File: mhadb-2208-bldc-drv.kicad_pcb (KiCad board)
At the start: 2 copper layers, 45 x 40 mm, 69 parts, among them J1 TC2030, J2 Conn_01x04, J3 Conn_01x04_Pin, M1 Motor_3_Phases, SW1 SW_Push, SW2 SW_Push, SW3 SW_Push, U1 SN65HVD230, U2 STM32F103C8Tx, U3 DRV8311H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

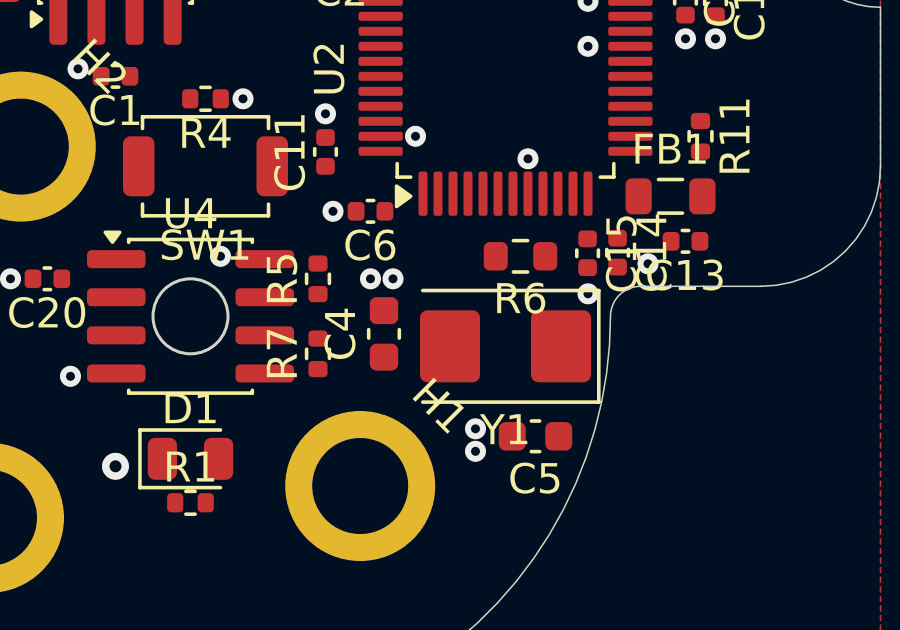
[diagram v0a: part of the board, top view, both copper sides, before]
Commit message: pcb: route crystal
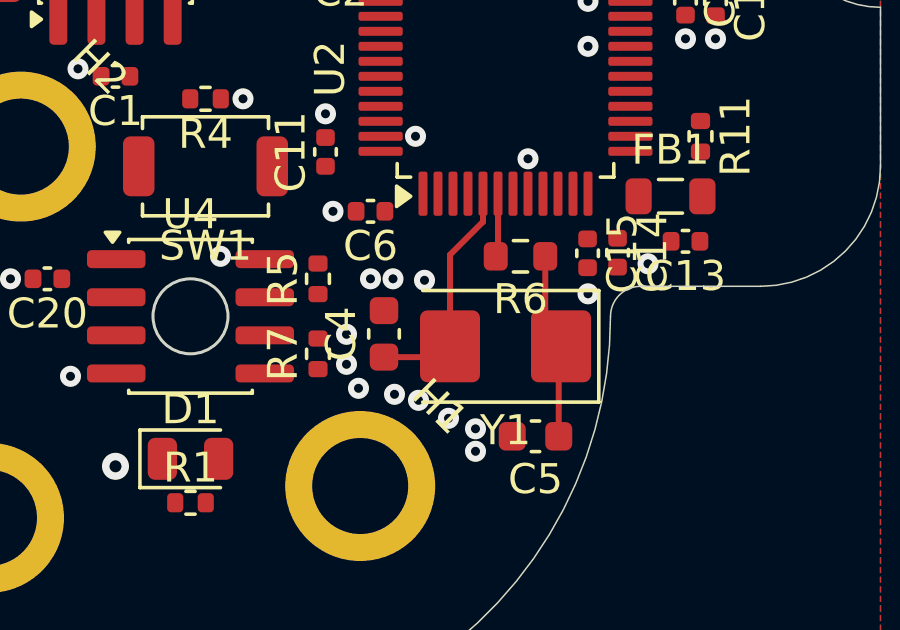
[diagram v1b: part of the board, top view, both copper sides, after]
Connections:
- U2 pad 25: /BTN1 -> unconnected-(U2-PB12-Pad25)
- U2 pad 41: unconnected-(U2-PB5-Pad41) -> /BTN1
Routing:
- net /XTAL_I: track 0.00 -> 7.89 mm
- net /XTAL_RO: track 0.00 -> 6.25 mm
- net /XTAL_O: track 0.00 -> 2.12 mm
- net GND: vias 53 -> 60
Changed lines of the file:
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@@
 	(net 41 "/SOB")
 	(net 42 "unconnected-(U1-Vref-Pad5)")
-	(net 43 "unconnected-(U2-PB5-Pad41)")
+	(net 43 "unconnected-(U2-PB12-Pad25)")
 	(net 44 "unconnected-(U2-PA7-Pad17)")
 	(net 45 "unconnected-(U2-PC13-Pad2)")
@@
 			(layers "F.Cu" "F.Mask" "F.Paste")
 			(roundrect_rratio 0.25)
-			(net 39 "/BTN1")
+			(net 43 "unconnected-(U2-PB12-Pad25)")
 			(pinfunction "PB12")
-			(pintype "bidirectional")
+			(pintype "bidirectional+no_connect")
 		)
 		(pad "26" smd roundrect
@@
 			(layers "F.Cu" "F.Mask" "F.Paste")
 			(roundrect_rratio 0.25)
-			(net 43 "unconnected-(U2-PB5-Pad41)")
+			(net 39 "/BTN1")
 			(pinfunction "PB5")
-			(pintype "bidirectional+no_connect")
+			(pintype "bidirectional")
 		)
 		(pad "42" smd roundrect
@@
 	)
 	(via
+		(at 124.6 88.4)
+		(size 0.7)
+		(drill 0.3)
+		(layers "F.Cu" "B.Cu")
+		(free yes)
+		(net 2)
+	)
+	(via
 		(at 120.75 78.75)
 		(size 0.7)
@@
 	)
 	(via
+		(at 127.6 89.4)
+		(size 0.7)
+		(drill 0.3)
+		(layers "F.Cu" "B.Cu")
+		(free yes)
+		(net 2)
+	)
+	(via
 		(at 124 70.5)
 		(size 0.9)
@@
 	)
 	(via
+		(at 124.2 86.6)
+		(size 0.7)
+		(drill 0.3)
+		(layers "F.Cu" "B.Cu")
+		(free yes)
+		(net 2)
+	)
+	(via
 		(at 134.25 65)
 		(size 0.7)
@@
 	)
 	(via
+		(at 126.8 84.8)
+		(size 0.7)
+		(drill 0.3)
+		(layers "F.Cu" "B.Cu")
+		(free yes)
+		(net 2)
+	)
+	(via
 		(at 102.25 76.25)
 		(size 0.7)
@@
 	)
 	(via
+		(at 124.2 87.6)
+		(size 0.7)
+		(drill 0.3)
+		(layers "F.Cu" "B.Cu")
+		(free yes)
+		(net 2)
+	)
+	(via
 		(at 128.5 90.5)
 		(size 0.7)
@@
 	)
 	(via
+		(at 126.6 88.8)
+		(size 0.7)
+		(drill 0.3)
+		(layers "F.Cu" "B.Cu")
+		(free yes)
+		(net 2)
+	)
+	(via
 		(at 105.25 70.5)
 		(size 0.7)
@@
 		(net 2)
 	)
+	(via
+		(at 125.8 88.6)
+		(size 0.7)
+		(drill 0.3)
+		(layers "F.Cu" "B.Cu")
+		(free yes)
+		(net 2)
+	)
+	(segment
+		(start 128.75 82.85)
+		(end 127.65 83.95)
+		(width 0.2)
+		(layer "F.Cu")
+		(net 5)
+	)
+	(segment
+		(start 127.65 83.95)
+		(end 127.65 87)
+		(width 0.2)
+		(layer "F.Cu")
+		(net 5)
+	)
+	(segment
+		(start 127.29 87.36)
+		(end 127.65 87)
+		(width 0.2)
+		(layer "F.Cu")
+		(net 5)
+	)
+	(segment
+		(start 128.75 81.9125)
+		(end 128.75 82.85)
+		(width 0.2)
+		(layer "F.Cu")
+		(net 5)
+	)
+	(segment
+		(start 125.45 87.36)
+		(end 127.29 87.36)
+		(width 0.2)
+		(layer "F.Cu")
+		(net 5)
+	)
+	(segment
+		(start 130.825 86.475)
+		(end 131.35 87)
+		(width 0.2)
+		(layer "F.Cu")
+		(net 6)
+	)
+	(segment
+		(start 131.275 87.075)
+		(end 131.35 87)
+		(width 0.2)
+		(layer "F.Cu")
+		(net 6)
+	)
+	(segment
+		(start 131.275 90)
+		(end 131.275 87.075)
+		(width 0.2)
+		(layer "F.Cu")
+		(net 6)
+	)
+	(segment
+		(start 130.825 84)
+		(end 130.825 86.475)
+		(width 0.2)
+		(layer "F.Cu")
+		(net 6)
+	)
+	(segment
+		(start 129.25 81.9125)
+		(end 129.25 83.925)
+		(width 0.2)
+		(layer "F.Cu")
+		(net 27)
+	)
+	(segment
+		(start 129.25 83.925)
+		(end 129.175 84)
+		(width 0.2)
+		(layer "F.Cu")
+		(net 27)
+	)
 	(zone

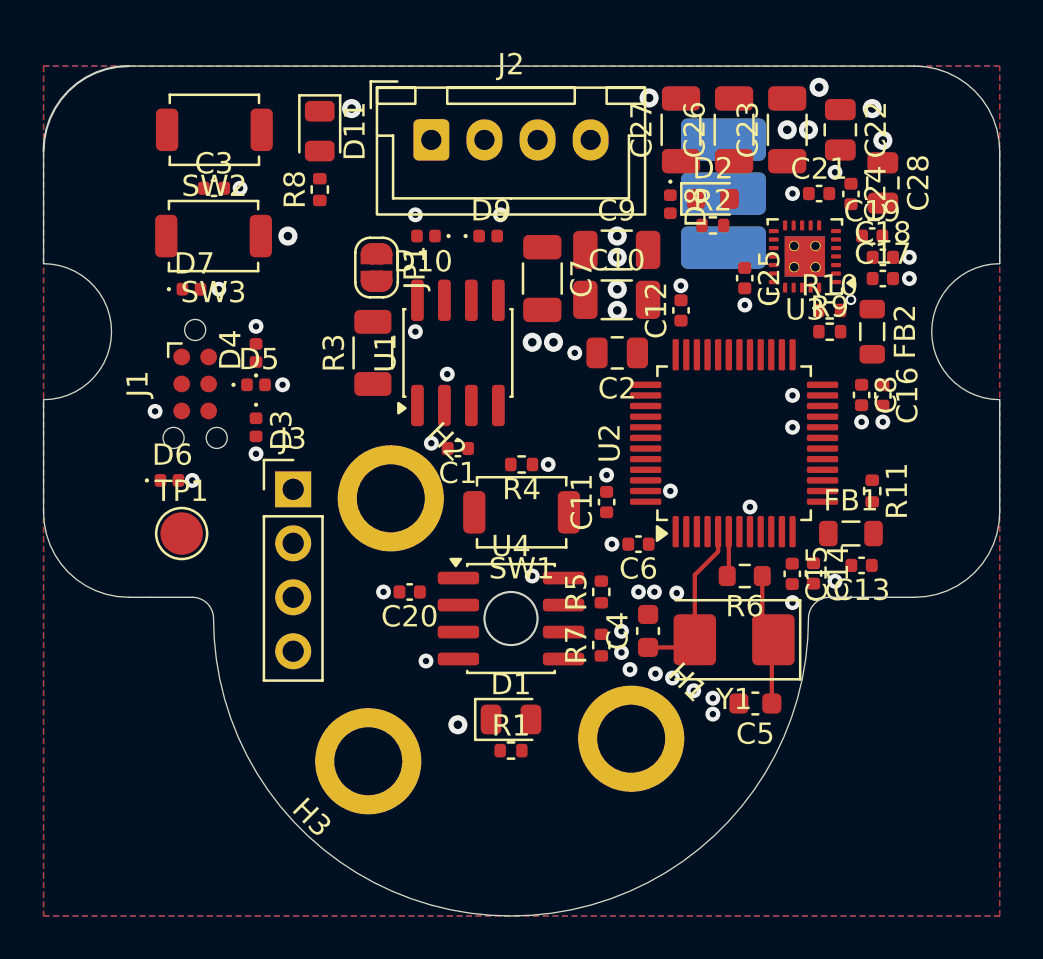
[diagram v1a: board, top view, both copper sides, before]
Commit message: pcb: route SWD
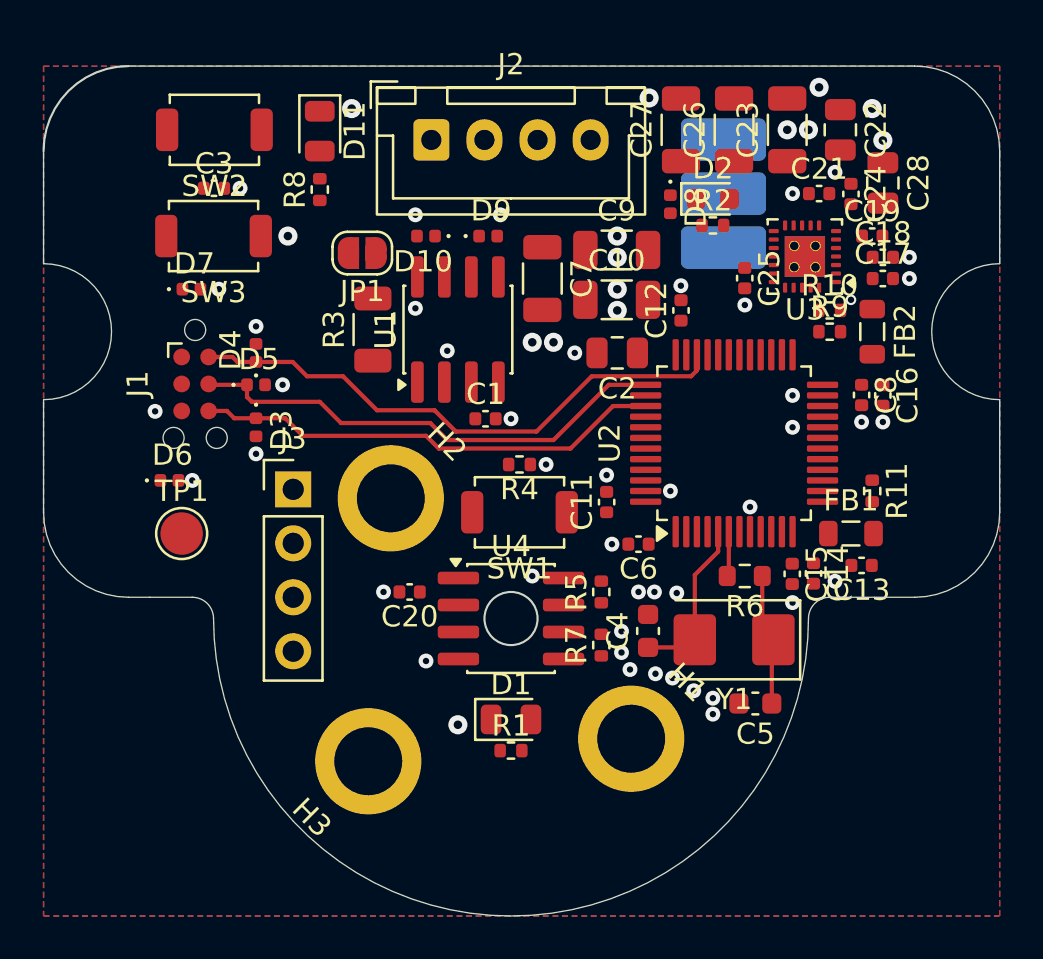
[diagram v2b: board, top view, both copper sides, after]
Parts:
- moved C1 1.91 mm to (117.8, 76.6), turned to 0 degrees
- moved R3 1.10 mm to (112.5, 72.4)
- moved U1 1.10 mm to (116.5, 72.4)
- moved JP1 0.96 mm to (112.0, 68.8), turned to 180 degrees
- moved R4 0.10 mm to (119.4, 78.8)
- moved SW1 0.10 mm to (119.4, 81.0)
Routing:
- net /SWDIO: track 0.00 -> 26.4 mm
- net /SWCLK: track 0.00 -> 23.1 mm
- net /SWO: track 0.00 -> 22.1 mm

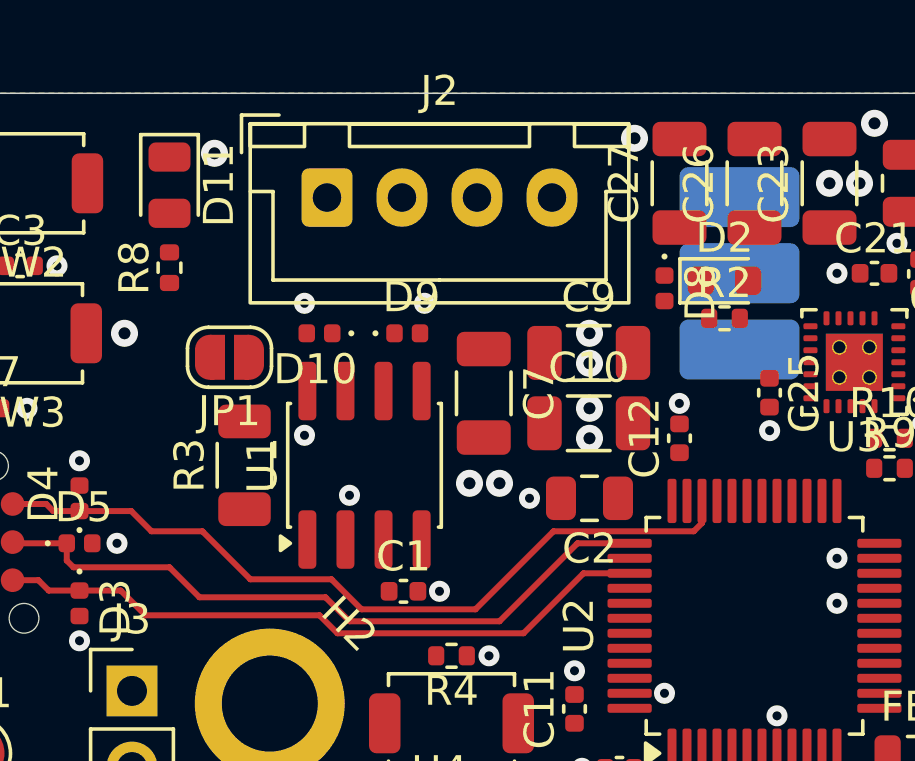
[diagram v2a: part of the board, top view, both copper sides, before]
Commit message: pcb: route CAN
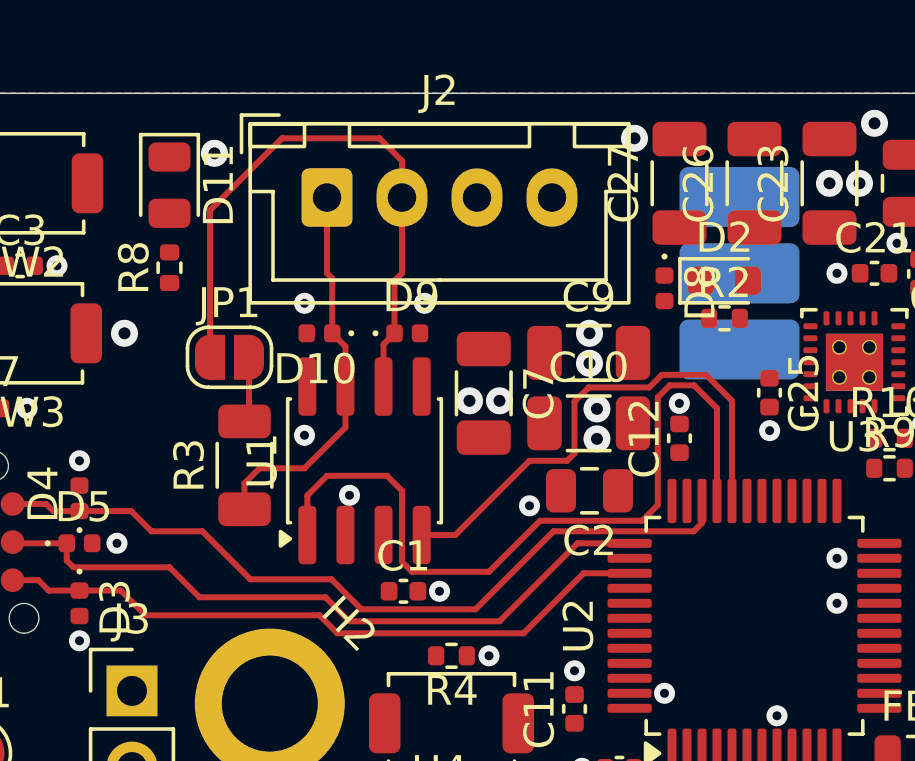
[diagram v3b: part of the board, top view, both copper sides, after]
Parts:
- moved C2 0.25 mm to (124.0, 73.2)
- moved U1 0.15 mm to (116.5, 72.2)
- turned JP1 to 0 degrees
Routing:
- net /CAN_TX: track 0.00 -> 26.0 mm
- net /CANL: track 0.00 -> 20.5 mm
- net /CAN_RX: track 0.00 -> 17.3 mm
- net /CANH: track 0.00 -> 13.1 mm
- net Net-(JP1-B): track 0.00 -> 2.41 mm

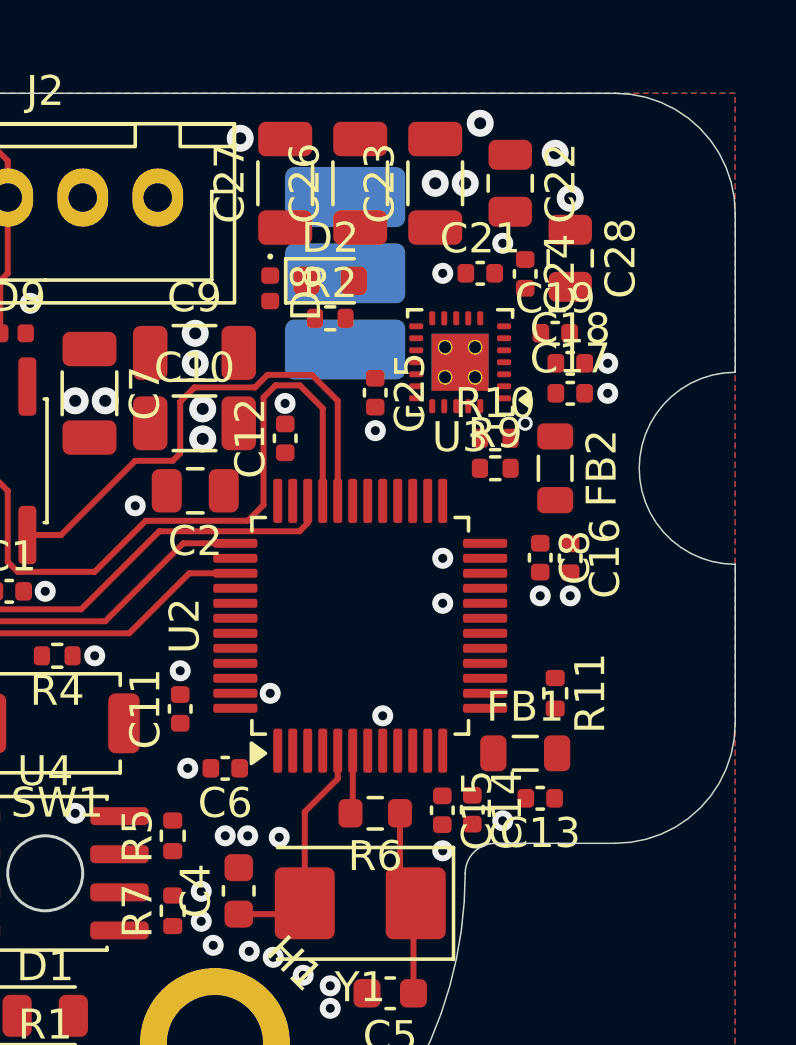
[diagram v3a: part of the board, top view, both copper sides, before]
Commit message: pcb: route DRV8311
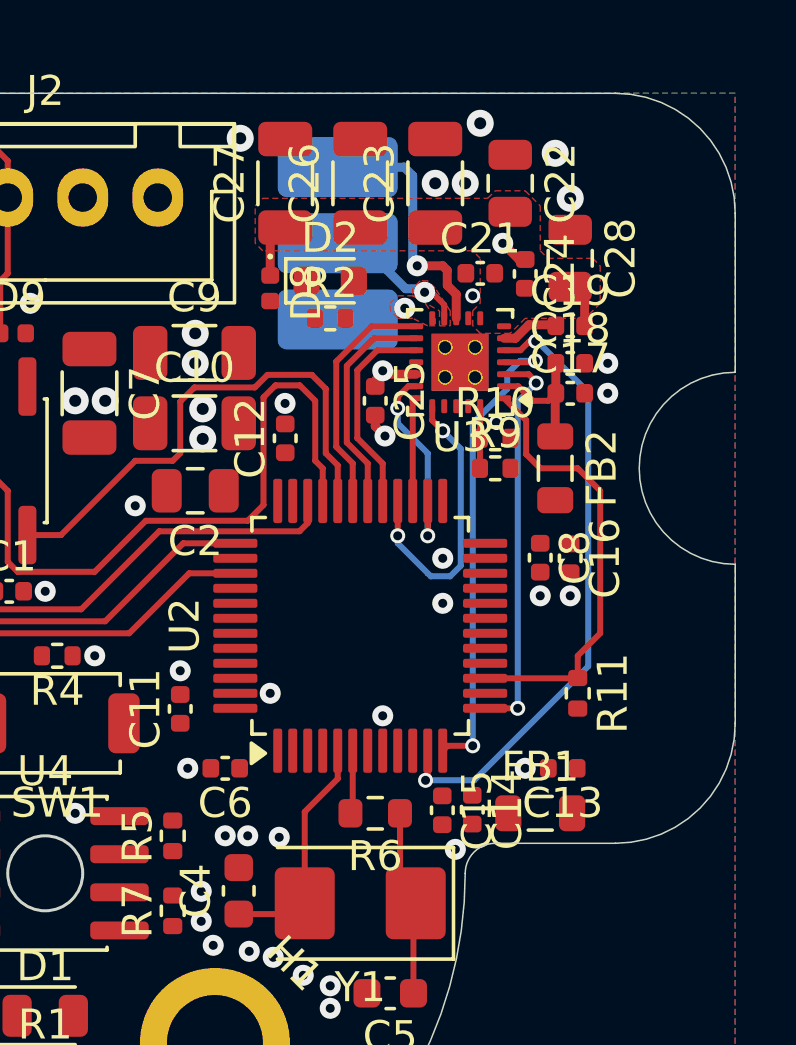
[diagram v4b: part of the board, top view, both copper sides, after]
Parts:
- moved FB1 2.06 mm to (135.5, 84.0)
- moved C13 1.25 mm to (136.2, 82.5)
- moved M1 1.03 mm to (128.8, 65.0)
- moved R11 0.75 mm to (136.8, 80.0)
- moved C19 0.56 mm to (136.5, 67.8)
- moved C25 0.27 mm to (130.0, 70.2)
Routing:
- net /SOA: track 0.00 -> 20.8 mm, vias 0 -> 2
- net /SOB: track 0.00 -> 16.1 mm, vias 0 -> 2
- net /~{FAULT}: track 0.00 -> 14.8 mm
- net /SOC: track 0.00 -> 13.4 mm, vias 0 -> 2
- net /INLC: track 0.00 -> 9.83 mm, vias 0 -> 2
- net Net-(U3-OUTA): track 0.00 -> 8.47 mm, vias 0 -> 1
- net /INHC: track 0.00 -> 8.03 mm
- net /INHB: track 0.00 -> 7.49 mm
- net /INLA: track 0.00 -> 6.97 mm, vias 0 -> 2
- net /INHA: track 0.00 -> 6.95 mm
- net Net-(U3-OUTB): track 0.00 -> 4.85 mm, vias 0 -> 1
- net Net-(U3-CSAREF): track 0.00 -> 4.48 mm
- net /INLB: track 0.00 -> 3.47 mm
- net +BATT: track 0.00 -> 3.31 mm
- net Net-(U3-OUTC): track 0.00 -> 2.39 mm, vias 0 -> 1
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- added copper zone on F.Cu, net +BATT
- added copper zone on F.Cu, net Net-(U3-OUTB)
- added copper zone on F.Cu, net Net-(U3-OUTC)

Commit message: pcb: route AS5600
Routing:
- net /SDA: track 0.00 -> 14.5 mm
- net /SCL: track 0.00 -> 13.5 mm
- net +3V3: track 1.79 -> 7.34 mm
- net GND: vias 60 -> 59
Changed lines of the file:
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@@
-	)
-	(via
-		(at 124.2 86.6)
-		(size 0.7)
-		(drill 0.3)
-		(layers "F.Cu" "B.Cu")
-		(free yes)
-		(net 2)
 	)
 	(via
@@
 	)
 	(segment
+		(start 115.365 85.365)
+		(end 116.525 85.365)
+		(width 0.3)
+		(layer "F.Cu")
+		(net 3)
+	)
+	(segment
+		(start 116.525 85.365)
+		(end 116.525 84.095)
+		(width 0.3)
+		(layer "F.Cu")
+		(net 3)
+	)
+	(segment
 		(start 130 69.5)
 		(end 130.25 69.25)
@@
 	)
 	(segment
+		(start 114.71 84.54)
+		(end 115.155 84.095)
+		(width 0.3)
+		(layer "F.Cu")
+		(net 3)
+	)
+	(segment
 		(start 131.365 69.365)
 		(end 130.365 69.365)
@@
 	)
 	(segment
+		(start 114.71 84.75)
+		(end 114.71 84.54)
+		(width 0.3)
+		(layer "F.Cu")
+		(net 3)
+	)
+	(segment
 		(start 130.365 69.365)
 		(end 130.25 69.25)
@@
 	)
 	(segment
+		(start 114.75 84.75)
+		(end 115.365 85.365)
+		(width 0.3)
+		(layer "F.Cu")
+		(net 3)
+	)
+	(segment
+		(start 114.71 84.75)
+		(end 114.75 84.75)
+		(width 0.3)
+		(layer "F.Cu")
+		(net 3)
+	)
+	(segment
 		(start 130 69.77)
 		(end 130 69.5)
@@
 		(net 3)
 	)
+	(segment
+		(start 115.155 84.095)
+		(end 116.525 84.095)
+		(width 0.3)
+		(layer "F.Cu")
+		(net 3)
+	)
 	(via
 		(at 130.25 69.25)
@@
 	)
 	(segment
+		(start 123.74 85.26)
+		(end 124 85)
+		(width 0.2)
+		(layer "F.Cu")
+		(net 24)
+	)
+	(segment
+		(start 124 83.75)
+		(end 123.75 83.5)
+		(width 0.2)
+		(layer "F.Cu")
+		(net 24)
+	)
+	(segment
+		(start 122.5 82.75)
+		(end 122.5 78.25)
+		(width 0.2)
+		(layer "F.Cu")
+		(net 24)
+	)
+	(segment
+		(start 123.25 85.26)
+		(end 123.74 85.26)
+		(width 0.2)
+		(layer "F.Cu")
+		(net 24)
+	)
+	(segment
+		(start 124 85)
+		(end 124 83.75)
+		(width 0.2)
+		(layer "F.Cu")
+		(net 24)
+	)
+	(segment
+		(start 121.58 85.26)
+		(end 121.475 85.365)
+		(width 0.2)
+		(layer "F.Cu")
+		(net 24)
+	)
+	(segment
+		(start 123.25 85.26)
+		(end 121.58 85.26)
+		(width 0.2)
+		(layer "F.Cu")
+		(net 24)
+	)
+	(segment
+		(start 122.5 78.25)
+		(end 123.25 77.5)
+		(width 0.2)
+		(layer "F.Cu")
+		(net 24)
+	)
+	(segment
+		(start 123.75 83.5)
+		(end 123.25 83.5)
+		(width 0.2)
+		(layer "F.Cu")
+		(net 24)
+	)
+	(segment
+		(start 123.25 77.5)
+		(end 125.3375 77.5)
+		(width 0.2)
+		(layer "F.Cu")
+		(net 24)
+	)
+	(segment
+		(start 123.25 83.5)
+		(end 122.5 82.75)
+		(width 0.2)
+		(layer "F.Cu")
+		(net 24)
+	)
+	(segment
+		(start 124.351 83.604611)
+		(end 123.895388 83.149)
+		(width 0.2)
+		(layer "F.Cu")
+		(net 25)
+	)
+	(segment
+		(start 123.25 86.74)
+		(end 121.58 86.74)
+		(width 0.2)
+		(layer "F.Cu")
+		(net 25)
+	)
+	(segment
+		(start 124.351 86.399)
+		(end 124.351 83.604611)
+		(width 0.2)
+		(layer "F.Cu")
+		(net 25)
+	)
+	(segment
+		(start 122.873194 78.626806)
+		(end 123.5 78)
+		(width 0.2)
+		(layer "F.Cu")
+		(net 25)
+	)
+	(segment
+		(start 122.873194 82.626806)
+		(end 122.873194 78.626806)
+		(width 0.2)
+		(layer "F.Cu")
+		(net 25)
+	)
+	(segment
+		(start 123.5 78)
+		(end 125.3375 78)
+		(width 0.2)
+		(layer "F.Cu")
+		(net 25)
+	)
+	(segment
+		(start 124.01 86.74)
+		(end 124.351 86.399)
+		(width 0.2)
+		(layer "F.Cu")
+		(net 25)
+	)
+	(segment
+		(start 123.395388 83.149)
+		(end 122.873194 82.626806)
+		(width 0.2)
+		(layer "F.Cu")
+		(net 25)
+	)
+	(segment
+		(start 123.895388 83.149)
+		(end 123.395388 83.149)
+		(width 0.2)
+		(layer "F.Cu")
+		(net 25)
+	)
+	(segment
+		(start 121.58 86.74)
+		(end 121.475 86.635)
+		(width 0.2)
+		(layer "F.Cu")
+		(net 25)
+	)
+	(segment
+		(start 123.25 86.74)
+		(end 124.01 86.74)
+		(width 0.2)
+		(layer "F.Cu")
+		(net 25)
+	)
+	(segment
